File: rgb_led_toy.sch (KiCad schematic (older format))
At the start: 25 parts, among them IC1 AT168, IC2 TS2940, P1 I2C, P2 I2C, P3 FTDI, P4 ISP, P5 VSEL, P6 ISP_E

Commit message: Testing feasibility of a ring with 3x MBI5168.
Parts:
- removed C4, C5: 10muF, symbol CP1
- removed IC2: TS2940, symbol LM1117
- removed P1, P2: I2C, symbol CONN_6
- removed P3: FTDI, symbol CONN_6
- removed P4: ISP, symbol CONN_3X2
- removed P5: VSEL, symbol CONN_3
- removed P6: ISP_E, symbol CONN_3X2
- removed R1: R, symbol R
- added C4, C5: 0.1µ, symbol C
- added IC2, IC3, IC4: MBI5168, symbol MBI5168
- added JP1: MADW__AVR_ISP, symbol MADW__AVR_ISP
- added MH1, MH2, MH3, MH4: CONN_1, symbol CONN_1
- added R4, R5: 600R, symbol R
- added RV1, RV2, RV3: 4k7, symbol POT
- C3: value 100nF -> 0.1µ
- R2: value R -> 10k
- R3: value R -> 600R
- renumbered R4 to R1
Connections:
- net labels added: LATCH, MISO, MOSI, O1.0, O1.1, O1.2, O1.3, O1.4, O1.5, O1.6, O1.7, O2.0, O2.1, O2.2, O2.3, O2.4, O2.5, O2.6, O2.7, O3.0, O3.1, O3.2, O3.3, O3.4, O3.5, O3.6, O3.7, OE, R.1, R.2, R.3, SCK
- net labels removed: ADC2, ADC3, BLUE, DTR, GREEN, MISO2/PB4, MOSI2/PB3, PB0, PB1, PB2, PB3/MOSI, PB4/MISO, PB5/SCK, PB6, PB7, RED, RXD, SCK2/PB5, SCL, SDA, TXD, V_in, V_reg
- wire segments 132 -> 69
- no-connect marks 0 -> 21
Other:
- moved on the sheet: C1, C2, D1, D2, D3, D4, D5, D6, D7, D8

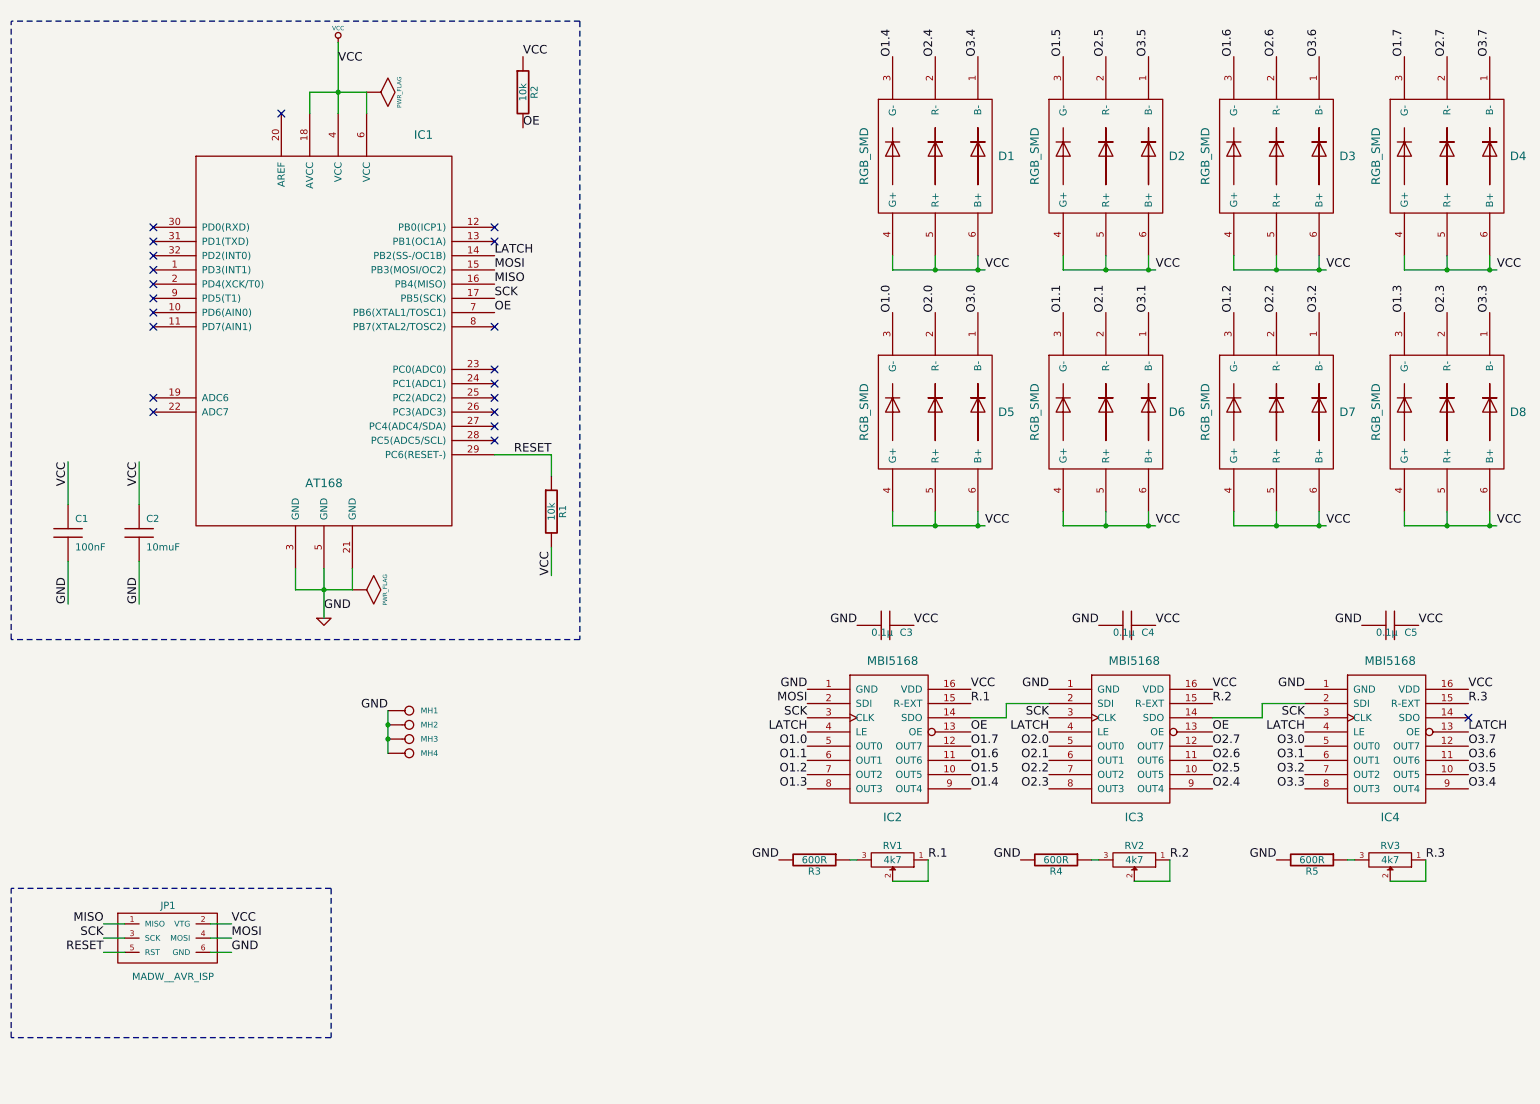
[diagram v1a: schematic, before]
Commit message: Version 2.0 alpha with just one MBI5168.
Let's see if color balancing can be done with software dot correction.
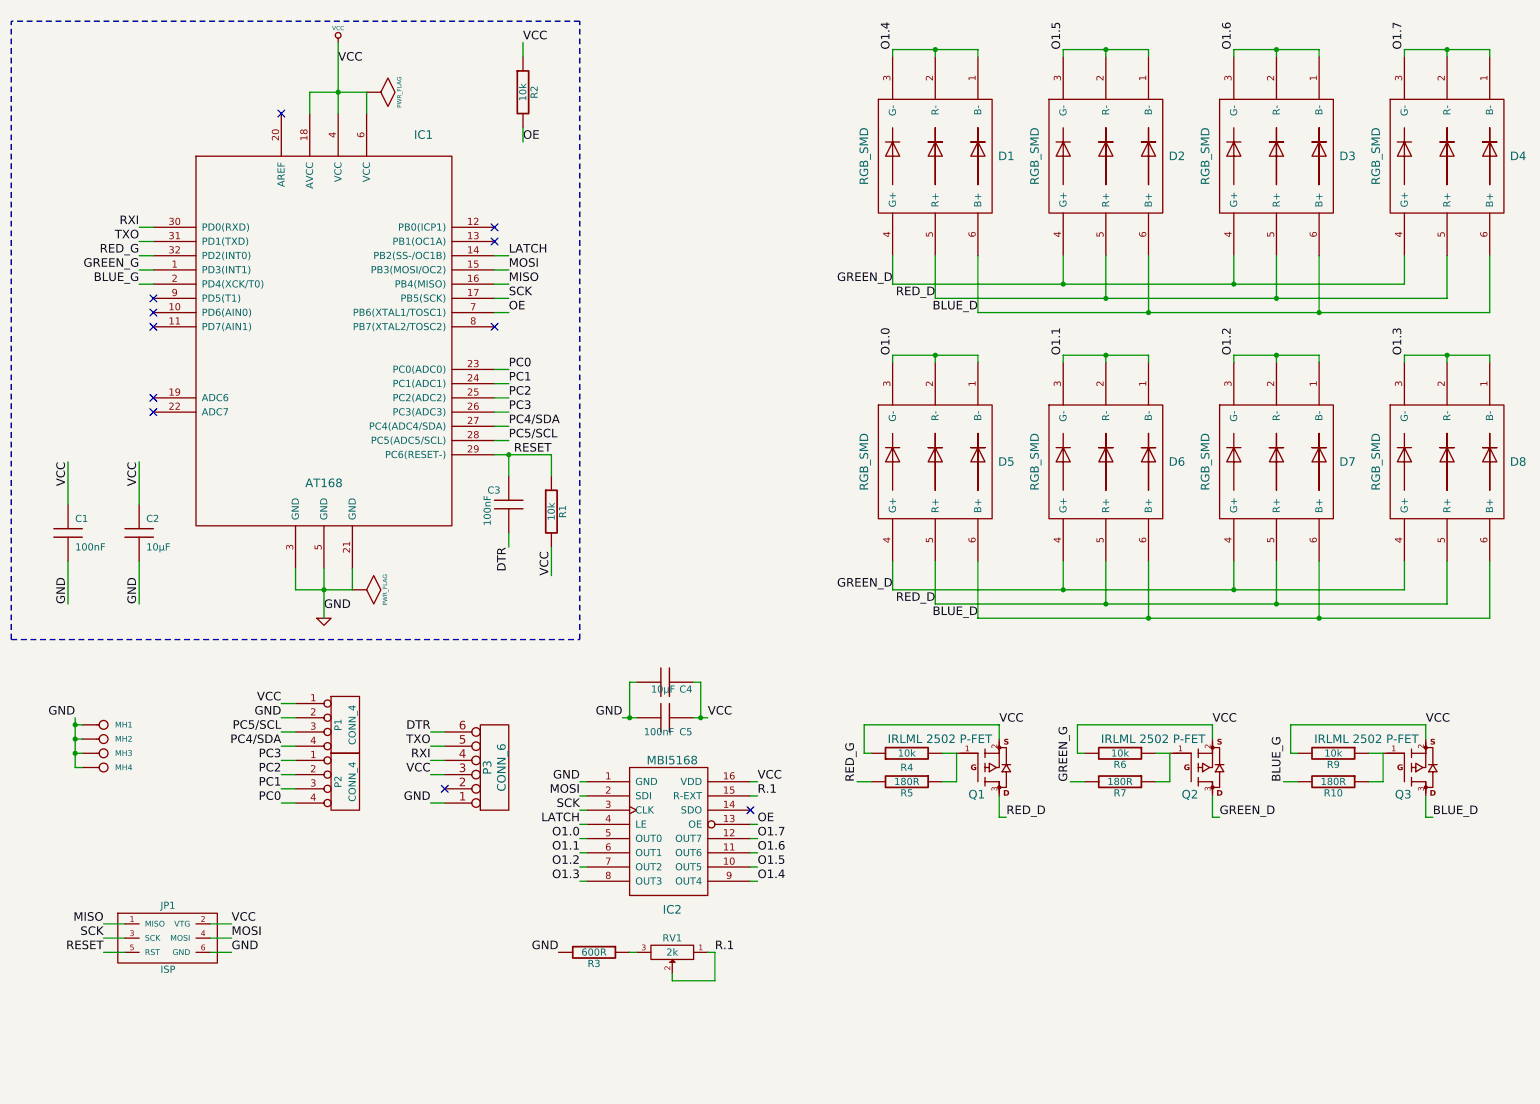
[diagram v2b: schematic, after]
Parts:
- removed C5: 0.1µ, symbol C
- removed IC3, IC4: MBI5168, symbol MBI5168
- removed RV2, RV3: 4k7, symbol POT
- added C3: 100nF, symbol C
- added P1, P2: CONN_4, symbol CONN_4
- added P3: CONN_6, symbol CONN_6
- added Q1, Q2, Q3: IRLML 2502 P-FET, symbol MOSFET_P
- added R10, R7: 180R, symbol R
- added R6, R9: 10k, symbol R
- C2: value 10muF -> 10µF
- C4: value 0.1µ -> 10µF
- C5: renamed from C3; value 0.1µ -> 100nF
- JP1: value MADW__AVR_ISP -> ISP
- R4: value 600R -> 10k
- R5: value 600R -> 180R
- RV1: value 4k7 -> 2k
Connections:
- net O2.0 is gone; now on net O1.0: D5.2 (R-)
- net O2.1 is gone; now on net O1.1: D6.2 (R-)
- net O2.2 is gone; now on net O1.2: D7.2 (R-)
- net O2.3 is gone; now on net O1.3: D8.2 (R-)
- net O2.4 is gone; now on net O1.4: D1.2 (R-)
- net O2.5 is gone; now on net O1.5: D2.2 (R-)
- net O2.6 is gone; now on net O1.6: D3.2 (R-)
- net O2.7 is gone; now on net O1.7: D4.2 (R-)
- net O3.0 is gone; now on net O1.0: D5.1 (B-)
- net O3.1 is gone; now on net O1.1: D6.1 (B-)
- net O3.2 is gone; now on net O1.2: D7.1 (B-)
- net O3.3 is gone; now on net O1.3: D8.1 (B-)
- net O3.4 is gone; now on net O1.4: D1.1 (B-)
- net O3.5 is gone; now on net O1.5: D2.1 (B-)
- net O3.6 is gone; now on net O1.6: D3.1 (B-)
- net O3.7 is gone; now on net O1.7: D4.1 (B-)
- net GND: now also P1.2 (P2), P3.1; no longer R4.2, R5.2
- net RESET: now also C3.1
- net VCC: now also R4.1, P1.1 (P1), P3.3, Q1.2 (S), Q2.2 (S), Q3.2 (S), R6.2, R9.2; no longer D1.4 (G+), D1.5 (R+), D1.6 (B+), D2.4 (G+), D2.5 (R+), D2.6 (B+), D3.4 (G+), D3.5 (R+), D3.6 (B+), D4.4 (G+), D4.5 (R+), D4.6 (B+), D5.4 (G+), D5.5 (R+), D5.6 (B+), D6.4 (G+), D6.5 (R+), D6.6 (B+), D7.4 (G+), D7.5 (R+), D7.6 (B+), D8.4 (G+), D8.5 (R+), D8.6 (B+)
- net GREEN_G: now reaches IC1.1 (PD3(INT1))
- net GREEN_G: now also R7.2
- net BLUE_G: now reaches IC1.2 (PD4(XCK/T0))
- net BLUE_G: now also R10.2
- net PC0: now reaches IC1.23 (PC0(ADC0))
- net PC0: now also P2.4 (P4)
- net PC1: now reaches IC1.24 (PC1(ADC1))
- net PC1: now also P2.3 (P3)
- net PC2: now reaches IC1.25 (PC2(ADC2))
- net PC2: now also P2.2 (P2)
- net PC3: now reaches IC1.26 (PC3(ADC3))
- net PC3: now also P2.1 (P1)
- net PC4/SDA: now reaches IC1.27 (PC4(ADC4/SDA))
- net PC4/SDA: now also P1.4 (P4)
- net PC5/SCL: now reaches IC1.28 (PC5(ADC5/SCL))
- net PC5/SCL: now also P1.3 (P3)
- net RXI: now reaches IC1.30 (PD0(RXD))
- net RXI: now also P3.4
- net TXO: now reaches IC1.31 (PD1(TXD))
- net TXO: now also P3.5
- net RED_G: now reaches IC1.32 (PD2(INT0))
- net RED_G: now also R5.2
- net at R5.1: now also R4.2, Q1.1 (G)
- new net: Q2.1 (G), R6.1, R7.1
- new net: Q3.1 (G), R10.1, R9.1
- new net BLUE_D: D1.6 (B+), D2.6 (B+), D3.6 (B+), D4.6 (B+), D5.6 (B+), D6.6 (B+), D7.6 (B+), D8.6 (B+), Q3.3 (D)
- new net DTR: C3.2, P3.6
- new net GREEN_D: D1.4 (G+), D2.4 (G+), D3.4 (G+), D4.4 (G+), D5.4 (G+), D6.4 (G+), D7.4 (G+), D8.4 (G+), Q2.3 (D)
- new net RED_D: D1.5 (R+), D2.5 (R+), D3.5 (R+), D4.5 (R+), D5.5 (R+), D6.5 (R+), D7.5 (R+), D8.5 (R+), Q1.3 (D)
- no-connect marks 21 -> 11
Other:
- moved on the sheet: C5, D5, D6, D7, D8, IC2, MH1, MH2, MH3, MH4, R3, RV1

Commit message: Fixd the LED numbering scheme.
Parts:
- renumbered D5 to D1, D6 to D2, D7 to D3, D8 to D4, D1 to D5, D2 to D6, D3 to D7, D4 to D8
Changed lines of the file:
@@
-EESchema Schematic File Version 2  date Tue 20 Dec 2011 01:42:05 PM CET
+EESchema Schematic File Version 2  date Tue 20 Dec 2011 02:44:46 PM CET
 LIBS:power
 LIBS:atmega8_168_328_TQFP
@@
 VCC
 $Comp
-L IMPOLUX_RGB_SMD D6
+L IMPOLUX_RGB_SMD D2
 U 1 1 49EB3626
 P 8250 3650
-F 0 "D6" H 8750 3650 60  0000 C CNN
+F 0 "D2" H 8750 3650 60  0000 C CNN
 F 1 "RGB_SMD" V 7750 3650 60  0000 C CNN
 	1    8250 3650
@@
 $EndComp
 $Comp
-L IMPOLUX_RGB_SMD D4
+L IMPOLUX_RGB_SMD D8
 U 1 1 49EB57EB
 P 10650 1500
-F 0 "D4" H 11150 1500 60  0000 C CNN
+F 0 "D8" H 11150 1500 60  0000 C CNN
 F 1 "RGB_SMD" V 10150 1500 60  0000 C CNN
 	1    10650 1500
@@
 O1.0
 $Comp
-L IMPOLUX_RGB_SMD D1
+L IMPOLUX_RGB_SMD D5
 U 1 1 49EB57EA
 P 7050 1500
-F 0 "D1" H 7550 1500 60  0000 C CNN
+F 0 "D5" H 7550 1500 60  0000 C CNN
 F 1 "RGB_SMD" V 6550 1500 60  0000 C CNN
 	1    7050 1500
@@
 $EndComp
 $Comp
-L IMPOLUX_RGB_SMD D7
+L IMPOLUX_RGB_SMD D3
 U 1 1 49EB3628
 P 9450 3650
-F 0 "D7" H 9950 3650 60  0000 C CNN
+F 0 "D3" H 9950 3650 60  0000 C CNN
 F 1 "RGB_SMD" V 8950 3650 60  0000 C CNN
 	1    9450 3650
@@
 $EndComp
 $Comp
-L IMPOLUX_RGB_SMD D5
+L IMPOLUX_RGB_SMD D1
 U 1 1 49EB3620
 P 7050 3650
-F 0 "D5" H 7550 3650 60  0000 C CNN
+F 0 "D1" H 7550 3650 60  0000 C CNN
 F 1 "RGB_SMD" V 6550 3650 60  0000 C CNN
 	1    7050 3650
@@
 $EndComp
 $Comp
-L IMPOLUX_RGB_SMD D3
+L IMPOLUX_RGB_SMD D7
 U 1 1 49EB57ED
 P 9450 1500
-F 0 "D3" H 9950 1500 60  0000 C CNN
+F 0 "D7" H 9950 1500 60  0000 C CNN
 F 1 "RGB_SMD" V 8950 1500 60  0000 C CNN
 	1    9450 1500
@@
 $EndComp
 $Comp
-L IMPOLUX_RGB_SMD D2
+L IMPOLUX_RGB_SMD D6
 U 1 1 49EB57EC
 P 8250 1500
-F 0 "D2" H 8750 1500 60  0000 C CNN
+F 0 "D6" H 8750 1500 60  0000 C CNN
 F 1 "RGB_SMD" V 7750 1500 60  0000 C CNN
 	1    8250 1500
@@
 $EndComp
 $Comp
-L IMPOLUX_RGB_SMD D8
+L IMPOLUX_RGB_SMD D4
 U 1 1 49EB3624
 P 10650 3650
-F 0 "D8" H 11150 3650 60  0000 C CNN
+F 0 "D4" H 11150 3650 60  0000 C CNN
 F 1 "RGB_SMD" V 10150 3650 60  0000 C CNN
 	1    10650 3650
